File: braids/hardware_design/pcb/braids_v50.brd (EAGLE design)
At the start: 78.7 x 106.7 mm, 120 parts, among them IC1 74HC595D, IC10 TL072, IC2 74HC595D, IC3 LM4040B25, IC4 MCP3204, IC5 DAC8551, IC6 LM1117-3.3, IC7 MCP6004, IC8 LM4040B10, IC9 TL074D, J1 PJ301_THONKICONN6, J2 PJ301_THONKICONN6, J3 PJ301_THONKICONN6, J4 PJ301_THONKICONN6, J5 PJ301_THONKICONN6, J6 PJ301_THONKICONN6, Q1 MMBT3904, Q2 MMBT3904, Q3 MMBT3904, Q4 MMBT3904, Q5 8MHz, Q6 MMBT3904, SW1 EC12E_SW

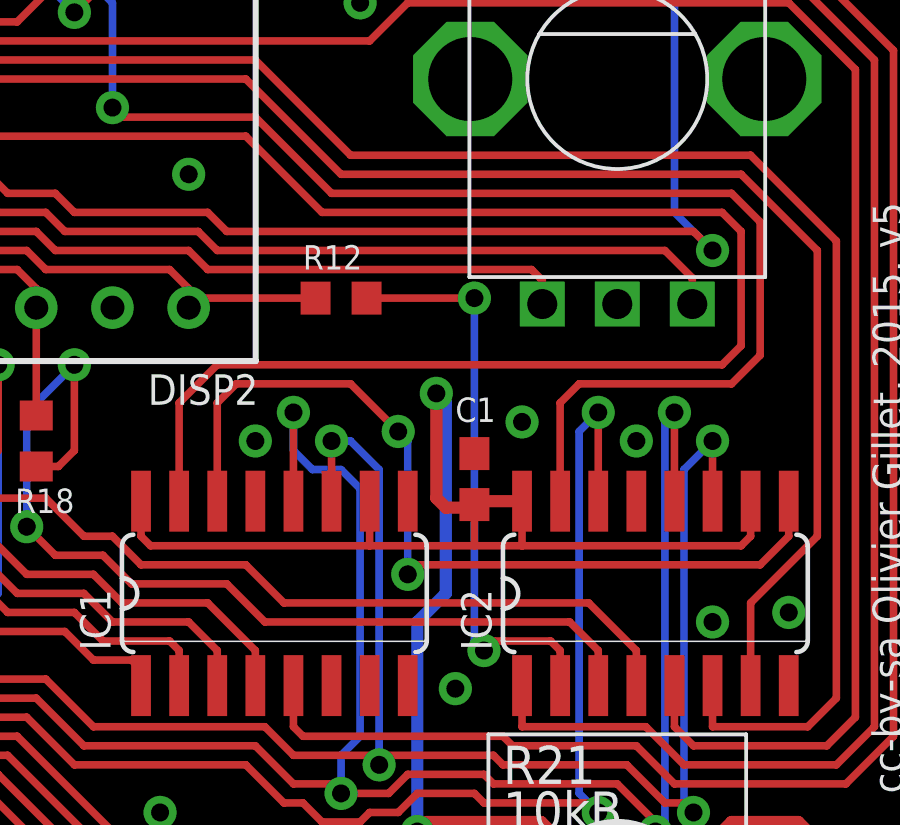
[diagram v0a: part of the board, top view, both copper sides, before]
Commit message: make the encoder A/B orientation a build time setting with solder jumpers
Signed-off-by: vladimir <vladimir@pantelic.net>
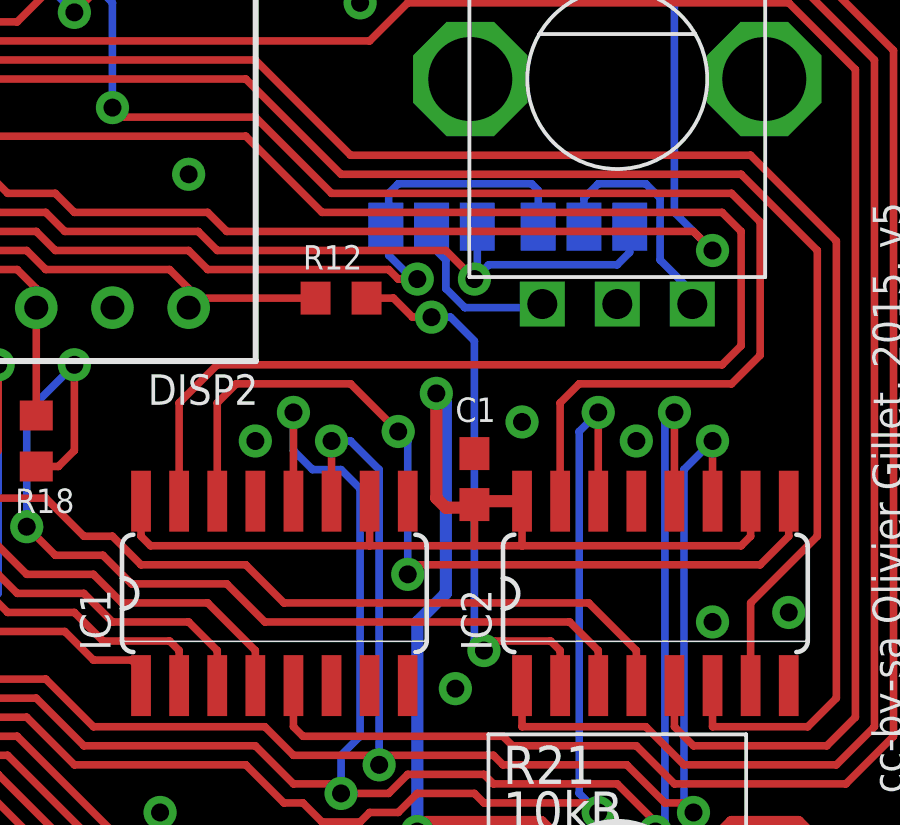
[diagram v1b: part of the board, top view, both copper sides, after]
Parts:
- added SJA, SJB: (no value), jumper:SJ_2
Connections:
- new net N$11: SJB.2, SW1.A
- new net N$76: SJA.2, SW1.B
- net ENC_A: now also SJA.1, SJB.3; no longer SW1.B
- net ENC_B: now also SJA.3, SJB.1; no longer SW1.A
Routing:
- net N$76: track 0.00 -> 7.86 mm
- net N$11: track 0.00 -> 5.79 mm
- net ENC_B: track 70.3 -> 75.1 mm, vias 2 -> 3
- net N$34: track 19.4 -> 18.6 mm
- net ENC_A: vias 2 -> 3
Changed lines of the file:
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@@
 <text x="77.7875" y="100.33" size="3.81" layer="26" ratio="15" rot="MR0">Braids</text>
 <text x="77.7875" y="98.7425" size="1.016" layer="26" ratio="15" rot="MR0">cc-by-sa Olivier Gillet, 2015. v5</text>
+<wire x1="64.4525" y1="86.6775" x2="66.9925" y2="86.6775" width="0.6096" layer="22"/>
+<wire x1="57.785" y1="86.6775" x2="60.325" y2="86.6775" width="0.6096" layer="22"/>
 </plain>
 <attributes>
@@
 <attribute name="VALUE" x="13.335" y="52.3875" size="0.8128" layer="27"/>
 </element>
+<element name="SJB" library="jumper" package="SJ_2" value="" x="59.84875" y="85.24875" smashed="yes" rot="MR180">
+<attribute name="NAME" x="59.563" y="87.3125" size="1.27" layer="26" ratio="10" rot="MR0"/>
+<attribute name="VALUE" x="59.74865" y="85.24875" size="0.02" layer="28" rot="MR180"/>
+</element>
+<element name="SJA" library="jumper" package="SJ_2" value="" x="64.92875" y="85.24875" smashed="yes" rot="MR0">
+<attribute name="NAME" x="66.548" y="87.3125" size="1.27" layer="26" ratio="10" rot="MR0"/>
+<attribute name="VALUE" x="65.02885" y="85.24875" size="0.02" layer="28" rot="MR0"/>
+</element>
 </elements>
 <signals>
@@
 </signal>
 <signal name="ENC_A">
-<contactref element="SW1" pad="B"/>
 <contactref element="UC1" pad="3"/>
 <wire x1="24.765" y1="59.69" x2="24.765" y2="60.96" width="0.254" layer="1"/>
@@
 <wire x1="47.625" y1="85.09" x2="52.07" y2="85.09" width="0.254" layer="1"/>
 <wire x1="52.07" y1="85.09" x2="52.705" y2="84.455" width="0.254" layer="1"/>
-<wire x1="52.705" y1="84.455" x2="67.6275" y2="84.455" width="0.254" layer="1"/>
+<wire x1="52.705" y1="84.455" x2="60.325" y2="84.455" width="0.254" layer="1"/>
 <wire x1="29.21" y1="88.265" x2="35.56" y2="88.265" width="0.254" layer="1"/>
 <wire x1="28.2575" y1="89.2175" x2="29.21" y2="88.265" width="0.254" layer="1"/>
@@
 <wire x1="24.765" y1="60.96" x2="25.0825" y2="61.2775" width="0.254" layer="16"/>
 <wire x1="25.0825" y1="61.2775" x2="25.0825" y2="88.265" width="0.254" layer="16"/>
-<wire x1="67.6275" y1="84.455" x2="68.54" y2="83.5425" width="0.254" layer="1"/>
-<wire x1="68.54" y1="83.5425" x2="68.54" y2="82.67" width="0.254" layer="1"/>
 <via x="24.765" y="59.69" extent="1-16" drill="0.6"/>
 <via x="25.0825" y="88.265" extent="1-16" drill="0.6"/>
+<contactref element="SJA" pad="1"/>
+<contactref element="SJB" pad="3"/>
+<wire x1="61.37275" y1="85.24875" x2="61.37275" y2="83.59775" width="0.254" layer="16"/>
+<wire x1="61.37275" y1="83.59775" x2="61.2775" y2="83.5025" width="0.254" layer="16"/>
+<via x="61.2775" y="83.5025" extent="1-16" drill="0.6"/>
+<wire x1="61.2775" y1="83.5025" x2="60.325" y2="84.455" width="0.254" layer="1"/>
+<wire x1="66.45275" y1="85.24875" x2="66.45275" y2="84.3915" width="0.254" layer="16"/>
+<wire x1="66.45275" y1="84.3915" x2="66.04" y2="83.97875" width="0.254" layer="16"/>
+<wire x1="66.04" y1="83.97875" x2="61.75375" y2="83.97875" width="0.254" layer="16"/>
+<wire x1="61.75375" y1="83.97875" x2="61.2775" y2="83.5025" width="0.254" layer="16"/>
 </signal>
 <signal name="ENC_B">
-<contactref element="SW1" pad="A"/>
 <contactref element="UC1" pad="4"/>
-<wire x1="63.1825" y1="83.82" x2="63.5" y2="83.5025" width="0.254" layer="1"/>
 <wire x1="25.7175" y1="60.6425" x2="25.7175" y2="61.2775" width="0.254" layer="1"/>
 <wire x1="25.7175" y1="60.6425" x2="25.7175" y2="80.3275" width="0.254" layer="16"/>
@@
 <wire x1="47.3075" y1="84.455" x2="51.7525" y2="84.455" width="0.254" layer="1"/>
 <wire x1="51.7525" y1="84.455" x2="52.3875" y2="83.82" width="0.254" layer="1"/>
-<wire x1="52.3875" y1="83.82" x2="63.1825" y2="83.82" width="0.254" layer="1"/>
+<wire x1="52.3875" y1="83.82" x2="58.42" y2="83.82" width="0.254" layer="1"/>
 <wire x1="25.7175" y1="80.3275" x2="27.6225" y2="82.2325" width="0.254" layer="16"/>
 <wire x1="27.6225" y1="82.2325" x2="27.6225" y2="88.265" width="0.254" layer="16"/>
 <wire x1="27.6225" y1="88.265" x2="28.2575" y2="87.63" width="0.254" layer="1"/>
 <wire x1="28.2575" y1="87.63" x2="35.2425" y2="87.63" width="0.254" layer="1"/>
-<wire x1="63.5" y1="83.5025" x2="63.54" y2="83.5025" width="0.254" layer="1"/>
-<wire x1="63.54" y1="83.5025" x2="63.54" y2="82.67" width="0.254" layer="1"/>
 <wire x1="25.7175" y1="61.2775" x2="25.42" y2="61.575" width="0.254" layer="1"/>
 <wire x1="25.42" y1="61.575" x2="25.42" y2="63.695" width="0.254" layer="1"/>
 <via x="25.7175" y="60.6425" extent="1-16" drill="0.6"/>
 <via x="27.6225" y="88.265" extent="1-16" drill="0.6"/>
+<contactref element="SJB" pad="1"/>
+<contactref element="SJA" pad="3"/>
+<via x="59.3725" y="83.5025" extent="1-16" drill="0.6"/>
+<wire x1="59.3725" y1="83.5025" x2="58.7375" y2="83.5025" width="0.254" layer="1"/>
+<wire x1="58.7375" y1="83.5025" x2="58.42" y2="83.82" width="0.254" layer="1"/>
+<wire x1="59.3725" y1="83.5025" x2="59.21375" y2="83.5025" width="0.254" layer="16"/>
+<wire x1="59.21375" y1="83.5025" x2="58.42" y2="84.29625" width="0.254" layer="16"/>
+<wire x1="58.42" y1="84.29625" x2="58.42" y2="85.1535" width="0.254" layer="16"/>
+<wire x1="58.42" y1="85.1535" x2="58.32475" y2="85.24875" width="0.254" layer="16"/>
+<wire x1="63.40475" y1="85.24875" x2="63.40475" y2="86.45525" width="0.254" layer="16"/>
+<wire x1="63.40475" y1="86.45525" x2="63.1825" y2="86.6775" width="0.254" layer="16"/>
+<wire x1="63.1825" y1="86.6775" x2="58.7375" y2="86.6775" width="0.254" layer="16"/>
+<wire x1="58.7375" y1="86.6775" x2="58.42" y2="86.36" width="0.254" layer="16"/>
+<wire x1="58.42" y1="86.36" x2="58.42" y2="85.344" width="0.254" layer="16"/>
+<wire x1="58.42" y1="85.344" x2="58.32475" y2="85.24875" width="0.254" layer="16"/>
 </signal>
 <signal name="ENC_CLICK">
@@
 <contactref element="R12" pad="1"/>
 <wire x1="61.595" y1="71.12" x2="61.2775" y2="71.4375" width="0.254" layer="16"/>
-<wire x1="61.2775" y1="71.4375" x2="61.2775" y2="82.8675" width="0.254" layer="16"/>
-<wire x1="61.2775" y1="82.8675" x2="57.6825" y2="82.8675" width="0.254" layer="1"/>
+<wire x1="61.2775" y1="71.4375" x2="61.2775" y2="81.43875" width="0.254" layer="16"/>
+<wire x1="58.57875" y1="82.8675" x2="57.6825" y2="82.8675" width="0.254" layer="1"/>
 <wire x1="64.135" y1="69.9516" x2="64.135" y2="71.12" width="0.254" layer="1"/>
 <wire x1="64.135" y1="71.12" x2="63.8175" y2="71.4375" width="0.254" layer="1"/>
@@
 <wire x1="61.9125" y1="71.4375" x2="61.595" y2="71.12" width="0.254" layer="1"/>
 <via x="61.595" y="71.12" extent="1-16" drill="0.6"/>
-<via x="61.2775" y="82.8675" extent="1-16" drill="0.6"/>
+<via x="59.84875" y="82.2325" extent="1-16" drill="0.6"/>
+<wire x1="61.2775" y1="81.43875" x2="60.48375" y2="82.2325" width="0.254" layer="16"/>
+<wire x1="60.48375" y1="82.2325" x2="59.84875" y2="82.2325" width="0.254" layer="16"/>
+<wire x1="58.57875" y1="82.8675" x2="59.21375" y2="82.2325" width="0.254" layer="1"/>
+<wire x1="59.21375" y1="82.2325" x2="59.84875" y2="82.2325" width="0.254" layer="1"/>
 </signal>
 <signal name="N$35">
@@
 <wire x1="12.7" y1="53.76" x2="12.7" y2="55.865" width="0.254" layer="1"/>
 </signal>
+<signal name="N$76">
+<contactref element="SW1" pad="B"/>
+<contactref element="SJA" pad="2"/>
+<wire x1="68.54" y1="82.67" x2="68.54" y2="83.06625" width="0.254" layer="16"/>
+<wire x1="68.54" y1="83.06625" x2="67.46875" y2="84.1375" width="0.254" layer="16"/>
+<wire x1="67.46875" y1="84.1375" x2="67.46875" y2="86.20125" width="0.254" layer="16"/>
+<wire x1="67.46875" y1="86.20125" x2="66.9925" y2="86.6775" width="0.254" layer="16"/>
+<wire x1="66.9925" y1="86.6775" x2="65.405" y2="86.6775" width="0.254" layer="16"/>
+<wire x1="65.405" y1="86.6775" x2="64.92875" y2="86.20125" width="0.254" layer="16"/>
+<wire x1="64.92875" y1="86.20125" x2="64.92875" y2="85.24875" width="0.254" layer="16"/>
+</signal>
+<signal name="N$11">
+<contactref element="SW1" pad="A"/>
+<contactref element="SJB" pad="2"/>
+<wire x1="59.84875" y1="84.61375" x2="59.84875" y2="85.24875" width="0.254" layer="16"/>
+<wire x1="59.84875" y1="84.61375" x2="60.325" y2="84.1375" width="0.254" layer="16"/>
+<wire x1="60.325" y1="84.1375" x2="60.325" y2="83.185" width="0.254" layer="16"/>
+<wire x1="60.325" y1="83.185" x2="60.96" y2="82.55" width="0.254" layer="16"/>
+<wire x1="60.96" y1="82.55" x2="63.42" y2="82.55" width="0.254" layer="16"/>
+<wire x1="63.42" y1="82.55" x2="63.54" y2="82.67" width="0.254" layer="16"/>
+</signal>
 </signals>
+<errors>
+</errors>
 </board>
 </drawing>

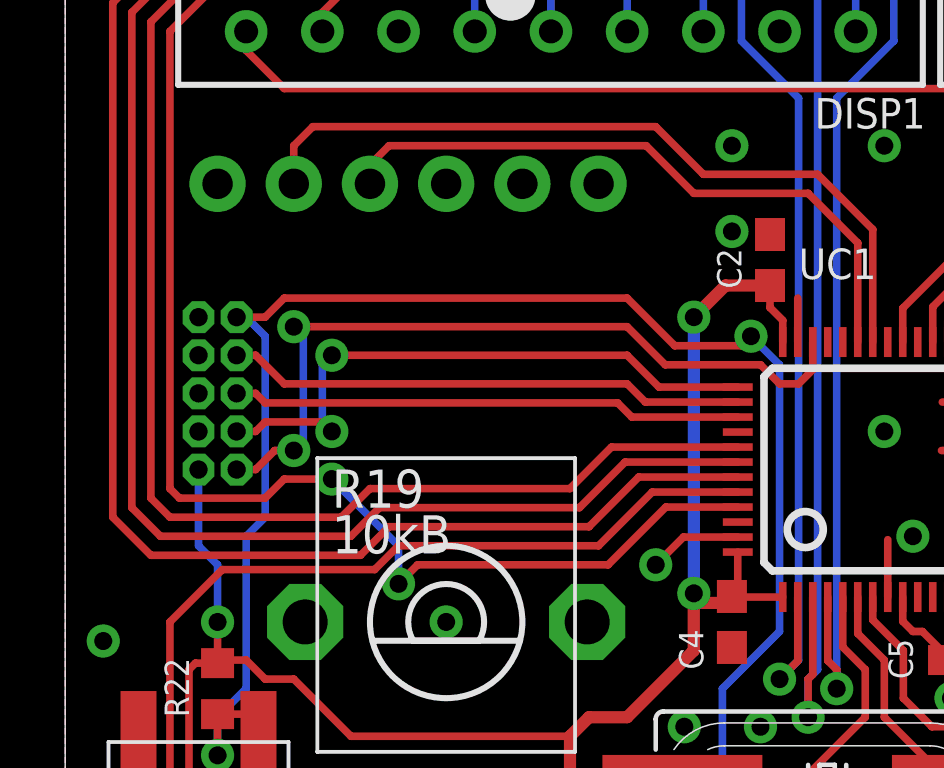
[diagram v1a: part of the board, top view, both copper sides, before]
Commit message: add a 6-pin combined SWD/UART header
Signed-off-by: Vladimir Pantelic <vladimir@pantelic.net>
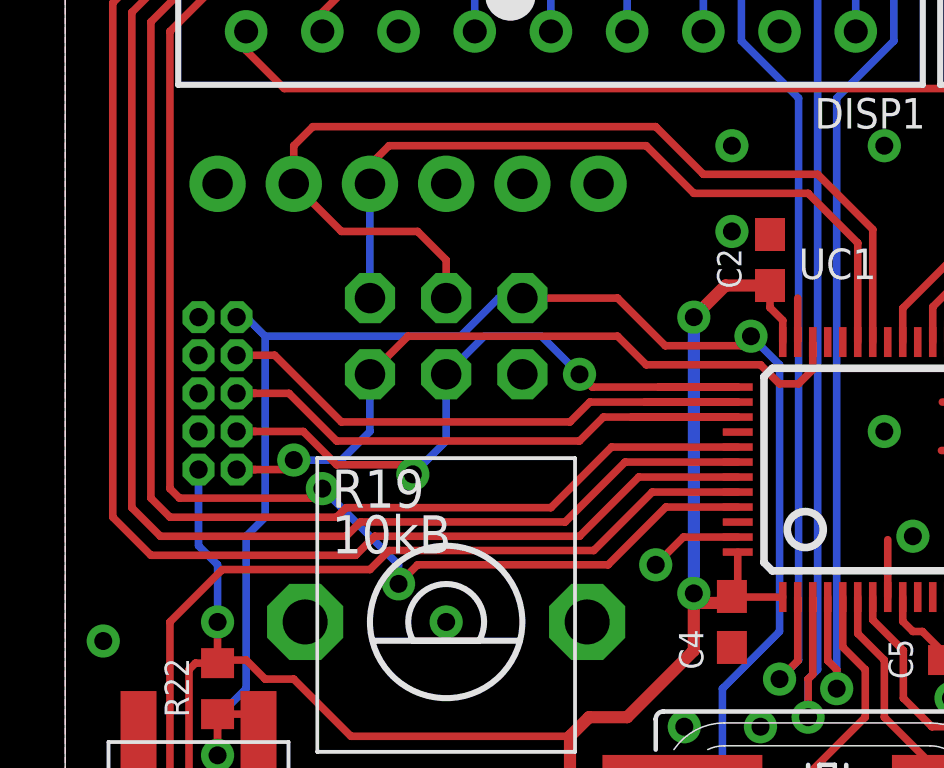
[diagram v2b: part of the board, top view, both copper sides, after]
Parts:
- added JP4: (no value), vpme_eurorack:2X03
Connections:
- net GND: now also JP4.1
- net JTCK: now also JP4.3
- net JTMS: now also JP4.5
- net RESET: now also JP4.2
- net RX: now also JP4.6
- net TX: now also JP4.4
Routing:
- net TX: track 26.0 -> 33.4 mm
- net JTDO: track 17.0 -> 21.9 mm
- net JTCK: track 20.4 -> 24.5 mm
- net RX: track 21.8 -> 25.6 mm
- net JTDI: track 17.4 -> 21.0 mm
- net JTMS: track 25.8 -> 24.6 mm, vias 2 -> 1
- net RESET: track 95.7 -> 95.0 mm
- net DISP_CHAR1: track 106.1 -> 105.5 mm
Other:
- board text added: "CLK"
- board text added: "DIO"
- board text added: "RST"
